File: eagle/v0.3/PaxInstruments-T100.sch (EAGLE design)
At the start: 30 parts, among them U1 Attiny85

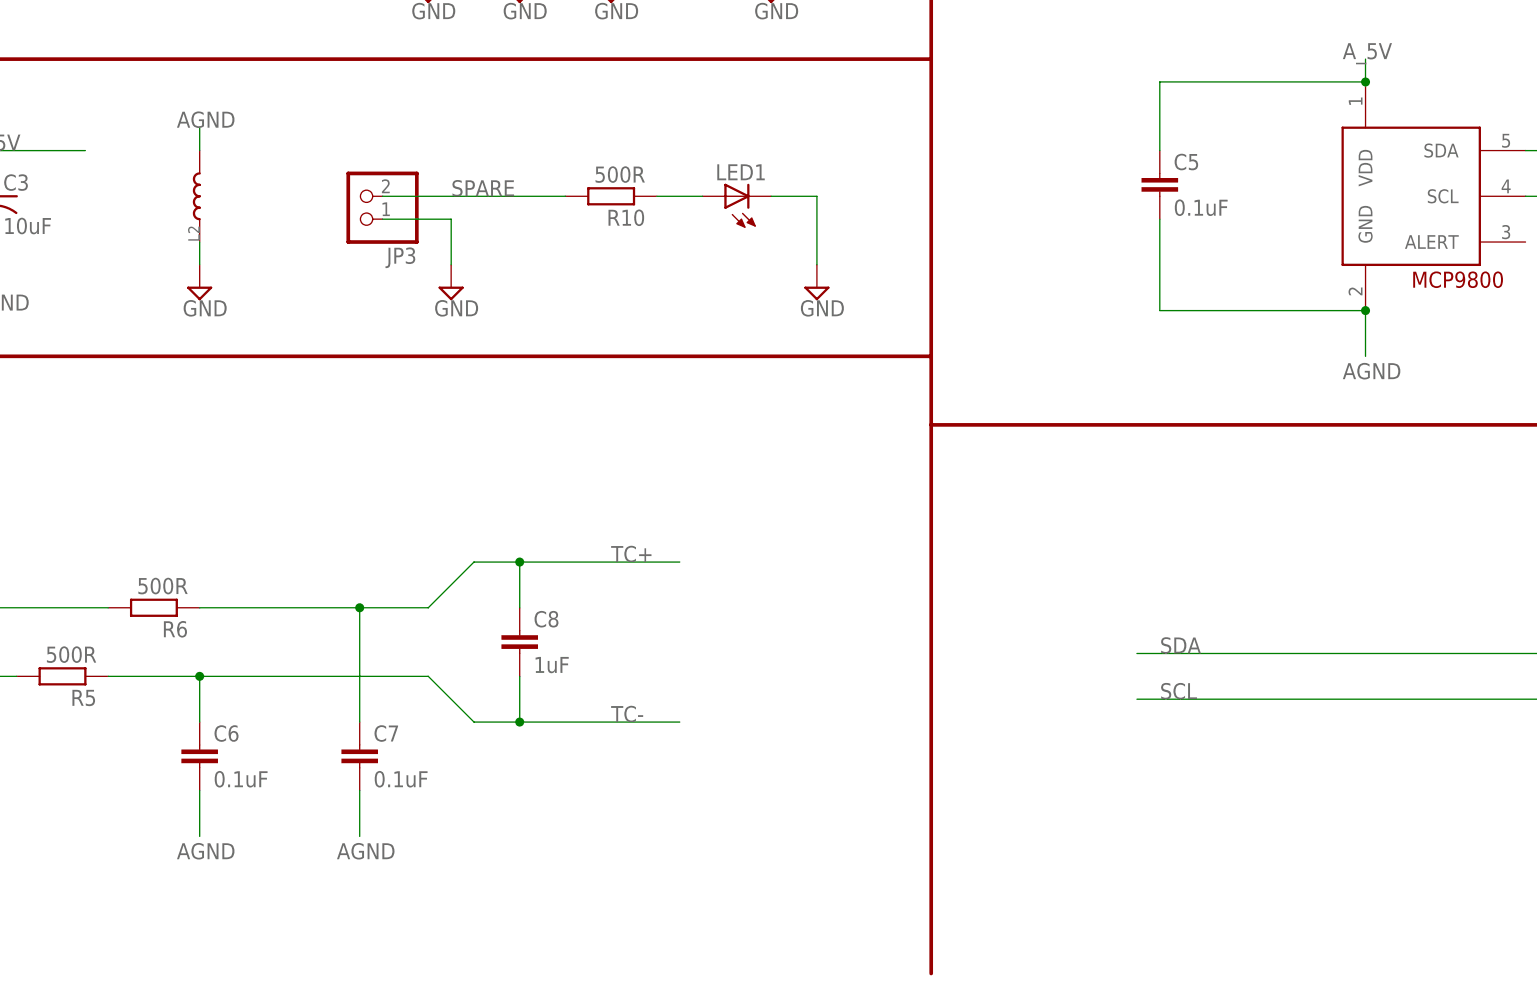
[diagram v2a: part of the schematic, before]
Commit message: New library added. Inductor changed to resistor. Logo placement.
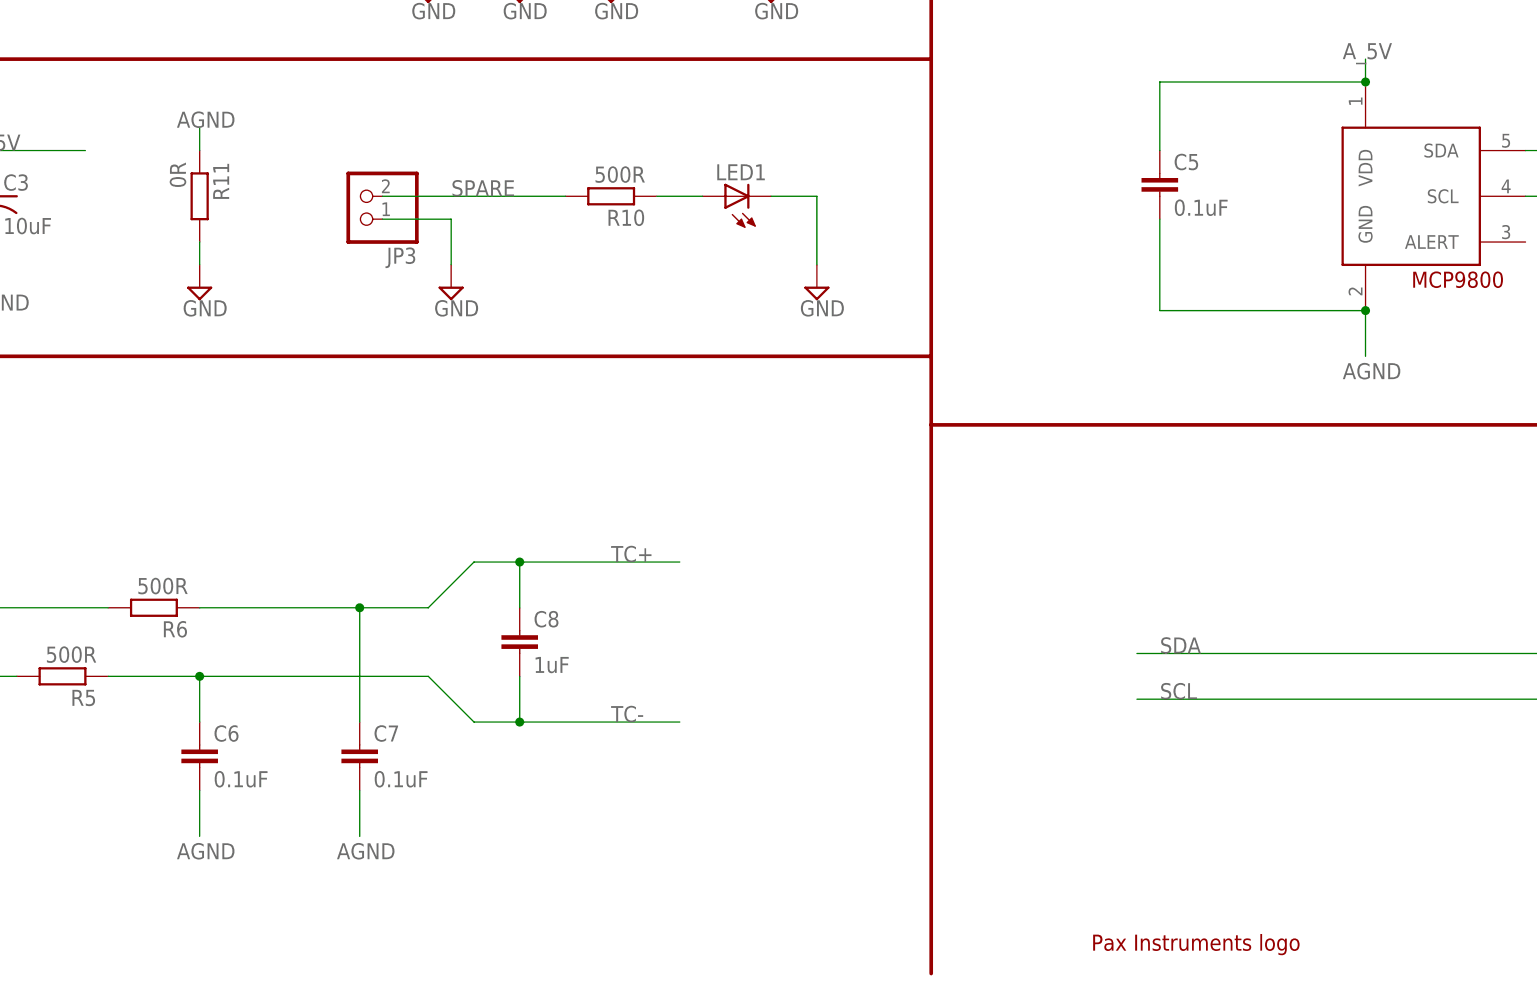
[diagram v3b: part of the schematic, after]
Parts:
- removed L2: (no value), SeeesStudio-OPL:L-0603
- added R11: 0R, rcl:R-EU_R0603
- added U$1: PAX-LOGOPAX-LOGO-0.25IN, PaxInstruments-Aesthetics:PAX-LOGOPAX-LOGO-0.25IN
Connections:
- net AGND: now also R11.1; no longer L2.2
- net GND: now also R11.2; no longer L2.1
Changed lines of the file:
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@@
 <grid distance="0.1" unitdist="inch" unit="inch" style="lines" multiple="1" display="no" altdistance="0.01" altunitdist="inch" altunit="inch"/>
 <layers>
-<layer number="1" name="Top" color="4" fill="1" visible="no" active="no"/>
-<layer number="16" name="Bottom" color="1" fill="1" visible="no" active="no"/>
-<layer number="17" name="Pads" color="2" fill="1" visible="no" active="no"/>
-<layer number="18" name="Vias" color="2" fill="1" visible="no" active="no"/>
-<layer number="19" name="Unrouted" color="6" fill="1" visible="no" active="no"/>
-<layer number="20" name="Dimension" color="15" fill="1" visible="no" active="no"/>
-<layer number="21" name="tPlace" color="7" fill="1" visible="no" active="no"/>
-<layer number="22" name="bPlace" color="7" fill="1" visible="no" active="no"/>
-<layer number="23" name="tOrigins" color="15" fill="1" visible="no" active="no"/>
-<layer number="24" name="bOrigins" color="15" fill="1" visible="no" active="no"/>
-<layer number="25" name="tNames" color="7" fill="1" visible="no" active="no"/>
-<layer number="26" name="bNames" color="7" fill="1" visible="no" active="no"/>
-<layer number="27" name="tValues" color="7" fill="1" visible="no" active="no"/>
-<layer number="28" name="bValues" color="7" fill="1" visible="no" active="no"/>
+<layer number="1" name="Top" color="4" fill="1" visible="yes" active="no"/>
+<layer number="16" name="Bottom" color="1" fill="1" visible="yes" active="no"/>
+<layer number="17" name="Pads" color="2" fill="1" visible="yes" active="no"/>
+<layer number="18" name="Vias" color="2" fill="1" visible="yes" active="no"/>
+<layer number="19" name="Unrouted" color="6" fill="1" visible="yes" active="no"/>
+<layer number="20" name="Dimension" color="15" fill="1" visible="yes" active="no"/>
+<layer number="21" name="tPlace" color="7" fill="1" visible="yes" active="no"/>
+<layer number="22" name="bPlace" color="7" fill="1" visible="yes" active="no"/>
+<layer number="23" name="tOrigins" color="15" fill="1" visible="yes" active="no"/>
+<layer number="24" name="bOrigins" color="15" fill="1" visible="yes" active="no"/>
+<layer number="25" name="tNames" color="7" fill="1" visible="yes" active="no"/>
+<layer number="26" name="bNames" color="7" fill="1" visible="yes" active="no"/>
+<layer number="27" name="tValues" color="7" fill="1" visible="yes" active="no"/>
+<layer number="28" name="bValues" color="7" fill="1" visible="yes" active="no"/>
 <layer number="29" name="tStop" color="7" fill="3" visible="no" active="no"/>
 <layer number="30" name="bStop" color="7" fill="6" visible="no" active="no"/>
@@
 <layer number="35" name="tGlue" color="7" fill="4" visible="no" active="no"/>
 <layer number="36" name="bGlue" color="7" fill="5" visible="no" active="no"/>
-<layer number="37" name="tTest" color="7" fill="1" visible="no" active="no"/>
-<layer number="38" name="bTest" color="7" fill="1" visible="no" active="no"/>
+<layer number="37" name="tTest" color="7" fill="1" visible="yes" active="no"/>
+<layer number="38" name="bTest" color="7" fill="1" visible="yes" active="no"/>
 <layer number="39" name="tKeepout" color="4" fill="11" visible="no" active="no"/>
 <layer number="40" name="bKeepout" color="1" fill="11" visible="no" active="no"/>
@@
 <layer number="44" name="Drills" color="7" fill="1" visible="no" active="no"/>
 <layer number="45" name="Holes" color="7" fill="1" visible="no" active="no"/>
-<layer number="46" name="Milling" color="3" fill="1" visible="no" active="no"/>
-<layer number="47" name="Measures" color="7" fill="1" visible="no" active="no"/>
-<layer number="48" name="Document" color="7" fill="1" visible="no" active="no"/>
-<layer number="49" name="Reference" color="7" fill="1" visible="no" active="no"/>
-<layer number="50" name="dxf" color="7" fill="1" visible="no" active="no"/>
-<layer number="51" name="tDocu" color="7" fill="1" visible="no" active="no"/>
-<layer number="52" name="bDocu" color="7" fill="1" visible="no" active="no"/>
-<layer number="53" name="tGND_GNDA" color="7" fill="9" visible="no" active="no"/>
-<layer number="54" name="bGND_GNDA" color="1" fill="9" visible="no" active="no"/>
-<layer number="56" name="wert" color="7" fill="1" visible="no" active="no"/>
+<layer number="46" name="Milling" color="3" fill="1" visible="yes" active="no"/>
+<layer number="47" name="Measures" color="7" fill="1" visible="yes" active="no"/>
+<layer number="48" name="Document" color="7" fill="1" visible="yes" active="no"/>
+<layer number="49" name="Reference" color="7" fill="1" visible="yes" active="no"/>
+<layer number="50" name="dxf" color="7" fill="1" visible="yes" active="no"/>
+<layer number="51" name="tDocu" color="7" fill="1" visible="yes" active="no"/>
+<layer number="52" name="bDocu" color="7" fill="1" visible="yes" active="no"/>
+<layer number="53" name="tGND_GNDA" color="7" fill="9" visible="yes" active="no"/>
+<layer number="54" name="bGND_GNDA" color="1" fill="9" visible="yes" active="no"/>
+<layer number="56" name="wert" color="7" fill="1" visible="yes" active="no"/>
 <layer number="90" name="Modules" color="5" fill="1" visible="yes" active="yes"/>
 <layer number="91" name="Nets" color="2" fill="1" visible="yes" active="yes"/>
@@
 <part name="SUPPLY8" library="supply2" deviceset="GND" device=""/>
 <part name="U$5" library="PaxInstruments-Connectors" deviceset="TC-MINI-INSIDE" device=""/>
-<part name="L2" library="SeeesStudio-OPL" deviceset="L*" device="-0603"/>
+<part name="U$1" library="PaxInstruments-Aesthetics" deviceset="PAX-LOGO" device="PAX-LOGO-0.25IN" value="PAX-LOGOPAX-LOGO-0.25IN"/>
+<part name="R11" library="rcl" deviceset="R-EU_" device="R0603" value="0R"/>
 </parts>
 <sheets>
@@
 <instance part="SUPPLY8" gate="GND" x="93.98" y="81.28"/>
 <instance part="U$5" gate="G$1" x="22.86" y="43.18"/>
-<instance part="L2" gate="L" x="66.04" y="91.44" rot="R90"/>
+<instance part="U$1" gate="G$1" x="165.1" y="7.62"/>
+<instance part="R11" gate="G$1" x="66.04" y="91.44" rot="R270"/>
 </instances>
 <busses>
@@
 <pinref part="SUPPLY7" gate="GND" pin="GND"/>
 <wire x1="66.04" y1="83.82" x2="66.04" y2="86.36" width="0.1524" layer="91"/>
-<pinref part="L2" gate="L" pin="1"/>
+<pinref part="R11" gate="G$1" pin="2"/>
 </segment>
 <segment>
@@
 <wire x1="66.04" y1="96.52" x2="66.04" y2="99.06" width="0.1524" layer="91"/>
 <label x="63.5" y="99.06" size="1.778" layer="95"/>
-<pinref part="L2" gate="L" pin="2"/>
-</segment>
-<segment>
+<pinref part="R11" gate="G$1" pin="1"/>
+</segment>
+<segment>

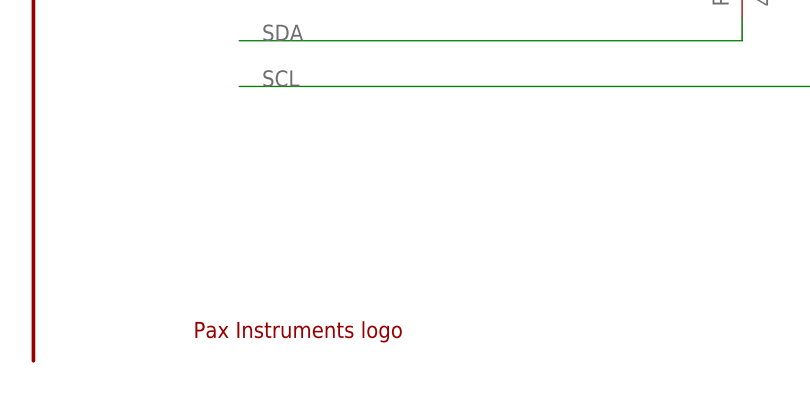
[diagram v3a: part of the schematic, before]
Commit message: Text label placements.
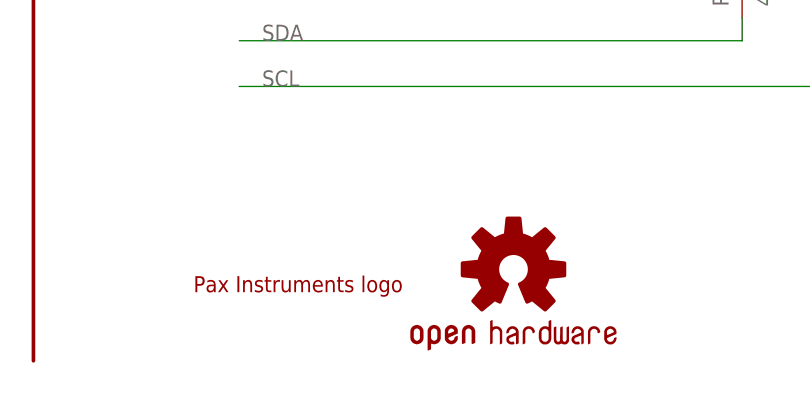
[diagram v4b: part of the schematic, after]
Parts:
- added LOGO1: SPARKFUN-AESTHETICS_OSHW-LOGOS, PaxInstrument-T400:SPARKFUN-AESTHETICS_OSHW-LOGOS
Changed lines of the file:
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@@
 <part name="U$1" library="PaxInstruments-Aesthetics" deviceset="PAX-LOGO" device="PAX-LOGO-0.25IN" value="PAX-LOGOPAX-LOGO-0.25IN"/>
 <part name="R11" library="rcl" deviceset="R-EU_" device="R0603" value="0R"/>
+<part name="LOGO1" library="PaxInstrument-T400" deviceset="SPARKFUN-AESTHETICS_OSHW-LOGO" device="S"/>
 </parts>
 <sheets>
@@
 <instance part="SUPPLY8" gate="GND" x="93.98" y="81.28"/>
 <instance part="U$5" gate="G$1" x="22.86" y="43.18"/>
-<instance part="U$1" gate="G$1" x="165.1" y="7.62"/>
+<instance part="U$1" gate="G$1" x="165.1" y="12.7"/>
 <instance part="R11" gate="G$1" x="66.04" y="91.44" rot="R270"/>
+<instance part="LOGO1" gate="G$1" x="200.66" y="15.24"/>
 </instances>
 <busses>

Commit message: Added MCP9800A0 part number. Closes #47.
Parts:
- U$4: value MCP9800 -> MCP9800A0
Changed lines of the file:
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@@
 <?xml version="1.0" encoding="utf-8"?>
 <!DOCTYPE eagle SYSTEM "eagle.dtd">
-<eagle version="7.3.0">
+<eagle version="7.2.0">
 <drawing>
 <settings>
@@
 <grid distance="0.1" unitdist="inch" unit="inch" style="lines" multiple="1" display="no" altdistance="0.01" altunitdist="inch" altunit="inch"/>
 <layers>
-<layer number="1" name="Top" color="4" fill="1" visible="yes" active="no"/>
-<layer number="16" name="Bottom" color="1" fill="1" visible="yes" active="no"/>
-<layer number="17" name="Pads" color="2" fill="1" visible="yes" active="no"/>
-<layer number="18" name="Vias" color="2" fill="1" visible="yes" active="no"/>
-<layer number="19" name="Unrouted" color="6" fill="1" visible="yes" active="no"/>
-<layer number="20" name="Dimension" color="15" fill="1" visible="yes" active="no"/>
-<layer number="21" name="tPlace" color="7" fill="1" visible="yes" active="no"/>
-<layer number="22" name="bPlace" color="7" fill="1" visible="yes" active="no"/>
-<layer number="23" name="tOrigins" color="15" fill="1" visible="yes" active="no"/>
-<layer number="24" name="bOrigins" color="15" fill="1" visible="yes" active="no"/>
-<layer number="25" name="tNames" color="7" fill="1" visible="yes" active="no"/>
-<layer number="26" name="bNames" color="7" fill="1" visible="yes" active="no"/>
-<layer number="27" name="tValues" color="7" fill="1" visible="yes" active="no"/>
-<layer number="28" name="bValues" color="7" fill="1" visible="yes" active="no"/>
+<layer number="1" name="Top" color="4" fill="1" visible="no" active="no"/>
+<layer number="16" name="Bottom" color="1" fill="1" visible="no" active="no"/>
+<layer number="17" name="Pads" color="2" fill="1" visible="no" active="no"/>
+<layer number="18" name="Vias" color="2" fill="1" visible="no" active="no"/>
+<layer number="19" name="Unrouted" color="6" fill="1" visible="no" active="no"/>
+<layer number="20" name="Dimension" color="15" fill="1" visible="no" active="no"/>
+<layer number="21" name="tPlace" color="7" fill="1" visible="no" active="no"/>
+<layer number="22" name="bPlace" color="7" fill="1" visible="no" active="no"/>
+<layer number="23" name="tOrigins" color="15" fill="1" visible="no" active="no"/>
+<layer number="24" name="bOrigins" color="15" fill="1" visible="no" active="no"/>
+<layer number="25" name="tNames" color="7" fill="1" visible="no" active="no"/>
+<layer number="26" name="bNames" color="7" fill="1" visible="no" active="no"/>
+<layer number="27" name="tValues" color="7" fill="1" visible="no" active="no"/>
+<layer number="28" name="bValues" color="7" fill="1" visible="no" active="no"/>
 <layer number="29" name="tStop" color="7" fill="3" visible="no" active="no"/>
 <layer number="30" name="bStop" color="7" fill="6" visible="no" active="no"/>
@@
 <layer number="35" name="tGlue" color="7" fill="4" visible="no" active="no"/>
 <layer number="36" name="bGlue" color="7" fill="5" visible="no" active="no"/>
-<layer number="37" name="tTest" color="7" fill="1" visible="yes" active="no"/>
-<layer number="38" name="bTest" color="7" fill="1" visible="yes" active="no"/>
+<layer number="37" name="tTest" color="7" fill="1" visible="no" active="no"/>
+<layer number="38" name="bTest" color="7" fill="1" visible="no" active="no"/>
 <layer number="39" name="tKeepout" color="4" fill="11" visible="no" active="no"/>
 <layer number="40" name="bKeepout" color="1" fill="11" visible="no" active="no"/>
@@
 <layer number="44" name="Drills" color="7" fill="1" visible="no" active="no"/>
 <layer number="45" name="Holes" color="7" fill="1" visible="no" active="no"/>
-<layer number="46" name="Milling" color="3" fill="1" visible="yes" active="no"/>
-<layer number="47" name="Measures" color="7" fill="1" visible="yes" active="no"/>
-<layer number="48" name="Document" color="7" fill="1" visible="yes" active="no"/>
-<layer number="49" name="Reference" color="7" fill="1" visible="yes" active="no"/>
-<layer number="50" name="dxf" color="7" fill="1" visible="yes" active="no"/>
-<layer number="51" name="tDocu" color="7" fill="1" visible="yes" active="no"/>
-<layer number="52" name="bDocu" color="7" fill="1" visible="yes" active="no"/>
-<layer number="53" name="tGND_GNDA" color="7" fill="9" visible="yes" active="no"/>
-<layer number="54" name="bGND_GNDA" color="1" fill="9" visible="yes" active="no"/>
-<layer number="56" name="wert" color="7" fill="1" visible="yes" active="no"/>
+<layer number="46" name="Milling" color="3" fill="1" visible="no" active="no"/>
+<layer number="47" name="Measures" color="7" fill="1" visible="no" active="no"/>
+<layer number="48" name="Document" color="7" fill="1" visible="no" active="no"/>
+<layer number="49" name="Reference" color="7" fill="1" visible="no" active="no"/>
+<layer number="50" name="dxf" color="7" fill="1" visible="no" active="no"/>
+<layer number="51" name="tDocu" color="7" fill="1" visible="no" active="no"/>
+<layer number="52" name="bDocu" color="7" fill="1" visible="no" active="no"/>
+<layer number="53" name="tGND_GNDA" color="7" fill="9" visible="no" active="no"/>
+<layer number="54" name="bGND_GNDA" color="1" fill="9" visible="no" active="no"/>
+<layer number="56" name="wert" color="7" fill="1" visible="no" active="no"/>
 <layer number="90" name="Modules" color="5" fill="1" visible="yes" active="yes"/>
 <layer number="91" name="Nets" color="2" fill="1" visible="yes" active="yes"/>
@@
 <part name="SUPPLY5" library="supply2" deviceset="GND" device=""/>
 <part name="U$3" library="SparkFun-DigitalIC" deviceset="MCP3421" device=""/>
-<part name="U$4" library="SparkFun-DigitalIC" deviceset="MCP9800" device=""/>
+<part name="U$4" library="SparkFun-DigitalIC" deviceset="MCP9800" device="" value="MCP9800A0"/>
 <part name="L1" library="SeeesStudio-OPL" deviceset="L*" device="-0603"/>
 <part name="C3" library="SparkFun-Capacitors" deviceset="10UF-TANT" device="" value="10uF"/>
